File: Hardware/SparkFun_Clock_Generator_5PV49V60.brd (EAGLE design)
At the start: 27.9 x 25.4 mm, 72 parts, among them U1 IDT_5P49V60_CLOCK_GENERATOR, Y1 16MHz

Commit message: Minor adjustments to schematic
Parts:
- moved U$36 0.25 mm to (24.3, 16.0)
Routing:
- net GND: vias 20 -> 21
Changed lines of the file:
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@@
 <drawing>
 <settings>
-<setting alwaysvectorfont="yes"/>
+<setting alwaysvectorfont="no"/>
 <setting verticaltext="up"/>
 </settings>
-<grid distance="0.05" unitdist="inch" unit="inch" style="lines" multiple="1" display="yes" altdistance="0.001" altunitdist="inch" altunit="inch"/>
+<grid distance="0.01" unitdist="inch" unit="inch" style="lines" multiple="1" display="yes" altdistance="0.001" altunitdist="inch" altunit="inch"/>
 <layers>
 <layer number="1" name="Top" color="4" fill="1" visible="yes" active="yes"/>
@@
 <layer number="37" name="tTest" color="7" fill="1" visible="no" active="yes"/>
 <layer number="38" name="bTest" color="7" fill="1" visible="no" active="yes"/>
-<layer number="39" name="tKeepout" color="4" fill="11" visible="yes" active="yes"/>
+<layer number="39" name="tKeepout" color="4" fill="11" visible="no" active="yes"/>
 <layer number="40" name="bKeepout" color="1" fill="11" visible="no" active="yes"/>
 <layer number="41" name="tRestrict" color="4" fill="10" visible="no" active="yes"/>
@@
 <layer number="45" name="Holes" color="7" fill="1" visible="yes" active="yes"/>
 <layer number="46" name="Milling" color="3" fill="1" visible="no" active="yes"/>
-<layer number="47" name="Measures" color="7" fill="1" visible="yes" active="yes"/>
+<layer number="47" name="Measures" color="7" fill="1" visible="no" active="yes"/>
 <layer number="48" name="Document" color="7" fill="1" visible="no" active="yes"/>
 <layer number="49" name="Reference" color="13" fill="1" visible="yes" active="yes"/>
@@
 <element name="U$34" library="Even more labels" package="CLKB13" value="" x="19.939" y="18.3642" smashed="yes" rot="R90"/>
 <element name="U$35" library="Labels" package="I_SUPER2_C-()-03" value="" x="5.7658" y="16.002" smashed="yes" rot="MR0"/>
-<element name="U$36" library="led" package="LED0" value="" x="24.5618" y="16.002" smashed="yes" rot="MR0"/>
+<element name="U$36" library="led" package="LED0" value="" x="24.3078" y="16.002" smashed="yes" rot="MR0"/>
 <element name="J7" library="SparkFun-Connectors" package="1X01_SMALL" value="" x="19.0246" y="20.2184" smashed="yes"/>
 <element name="J8" library="SparkFun-Connectors" package="1X01_SMALL" value="" x="19.05" y="17.78" smashed="yes"/>
@@
 <via x="19.1262" y="18.7452" extent="1-16" drill="0.381"/>
 <via x="16.51" y="20.2946" extent="1-16" drill="0.381"/>
+<via x="16.6116" y="6.4516" extent="1-16" drill="0.381"/>
 </signal>
 <signal name="3.3V">
@@
 <wire x1="15.7988" y1="13.5382" x2="16.7386" y2="12.5984" width="0.2032" layer="16"/>
 <contactref element="J3" pad="8"/>
-<wire x1="24.3332" y1="3.6068" x2="25.008" y2="3.6068" width="0.2032" layer="16"/>
-<wire x1="16.7386" y1="12.5984" x2="16.7386" y2="11.2014" width="0.2032" layer="16"/>
-<wire x1="16.7386" y1="11.2014" x2="24.3332" y2="3.6068" width="0.2032" layer="16"/>
+<wire x1="24.8412" y1="3.6068" x2="25.008" y2="3.6068" width="0.2032" layer="16"/>
+<wire x1="16.7386" y1="12.5984" x2="16.7386" y2="11.7094" width="0.2032" layer="16"/>
+<wire x1="16.7386" y1="11.7094" x2="24.8412" y2="3.6068" width="0.2032" layer="16"/>
 </signal>
 <signal name="OUT1B">

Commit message: Removes pulling SEL_I2CB line from ground, and instead leaves it floating
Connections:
- new net SEL_I2CB: U1.P24
- net GND: no longer U1.P24
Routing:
- net GND: track 13.2 -> 8.49 mm, vias 21 -> 20
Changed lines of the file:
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@@
 <vertex x="-1.27" y="0"/>
 </polygon>
-<contactref element="U1" pad="P24"/>
 <contactref element="J4" pad="1"/>
 <contactref element="J1" pad="1"/>
@@
 <contactref element="C7" pad="2"/>
 <via x="10.3378" y="16.8402" extent="1-16" drill="0.381"/>
-<wire x1="14.6" y1="15.728" x2="14.62" y2="15.748" width="0.254" layer="1"/>
-<wire x1="14.62" y1="15.748" x2="15.5194" y2="15.748" width="0.254" layer="1"/>
-<wire x1="15.5194" y1="15.748" x2="16.129" y2="16.3576" width="0.254" layer="1"/>
 <via x="19.7358" y="12.9794" extent="1-16" drill="0.381"/>
 <via x="23.0632" y="11.2014" extent="1-16" drill="0.381"/>
-<via x="18.2372" y="16.7894" extent="1-16" drill="0.381"/>
 <via x="11.5316" y="21.3106" extent="1-16" drill="0.381"/>
 <via x="6.1214" y="14.9098" extent="1-16" drill="0.381"/>
 <via x="6.0706" y="16.383" extent="1-16" drill="0.381"/>
 <via x="6.3754" y="19.7358" extent="1-16" drill="0.381"/>
-<wire x1="17.8054" y1="16.3576" x2="18.2372" y2="16.7894" width="0.254" layer="1"/>
-<wire x1="16.129" y1="16.3576" x2="17.8054" y2="16.3576" width="0.254" layer="1"/>
 <wire x1="12.7" y1="14.478" x2="11.45" y2="15.728" width="0.254" layer="1"/>
 <wire x1="11.45" y1="15.728" x2="11.45" y2="16.378" width="0.254" layer="1"/>
 <wire x1="12.7" y1="14.478" x2="13.95" y2="15.728" width="0.254" layer="1"/>
-<wire x1="13.95" y1="15.728" x2="14.6" y2="15.728" width="0.254" layer="1"/>
 <via x="19.3802" y="14.1986" extent="1-16" drill="0.381"/>
 <wire x1="11.45" y1="16.378" x2="11.45" y2="16.998" width="0.254" layer="1"/>
@@
 <wire x1="25.4896" y1="18.2372" x2="25.4896" y2="17.3404" width="0.2032" layer="1"/>
 </signal>
+<signal name="SEL_I2CB">
+<contactref element="U1" pad="P24"/>
+</signal>
 </signals>

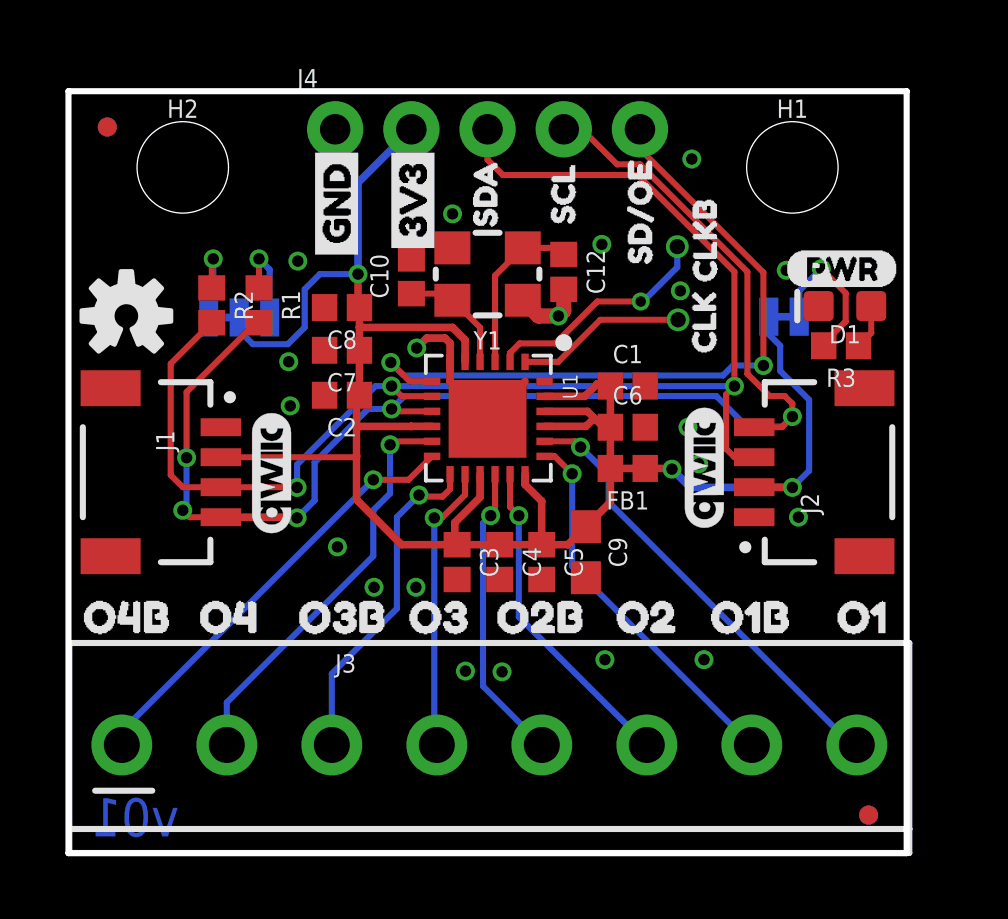
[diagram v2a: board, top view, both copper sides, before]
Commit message: Removes screw terminals in place of PTH header (with additional ground through holes)
* Adds better silk that...just makes more sense
* Adds ground vias to ground pad under IC
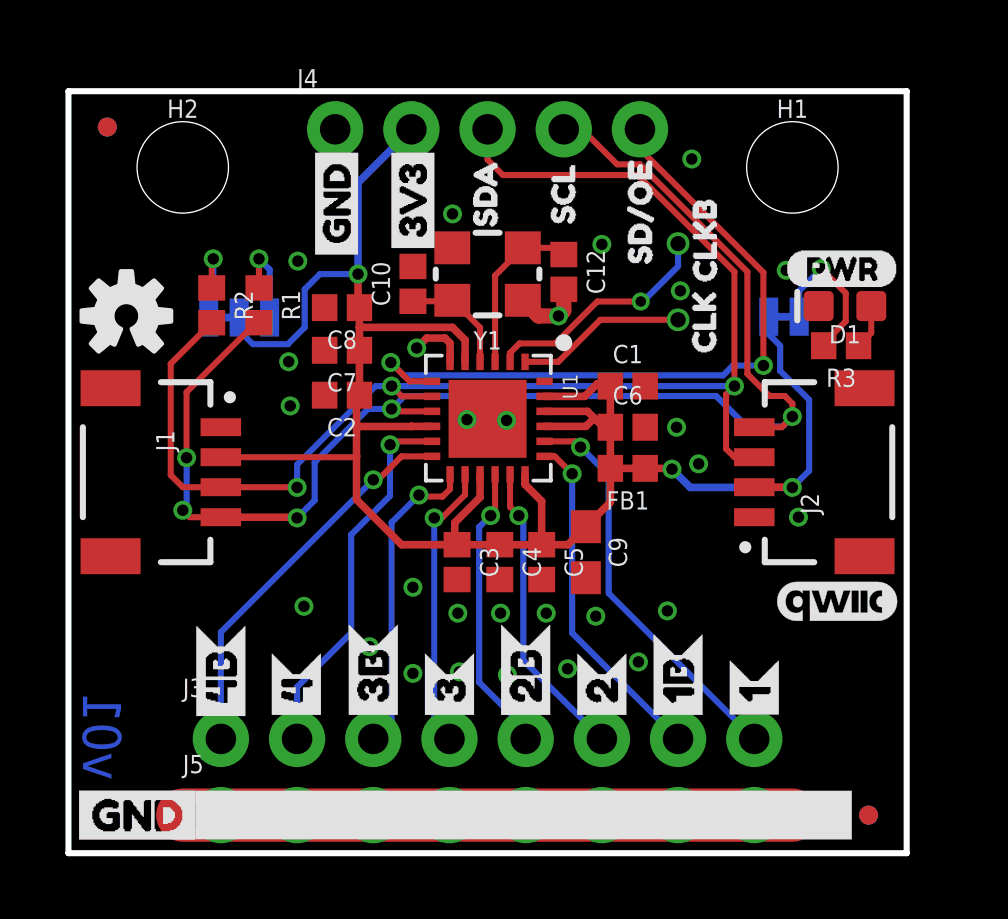
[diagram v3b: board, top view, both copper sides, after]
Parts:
- removed U$1: (no value), SparkFun-Aesthetics:QWIIC_4MM
- added J5: (no value), SparkFun-Connectors:1X08_NO_SILK
- added U$37: (no value), Top clock labels:34
- added U$38: (no value), Top clock labels:46
- J3: device SparkFun-Connectors:SCREWTERMINAL-3.5MM-8 -> SparkFun-Connectors:1X08_NO_SILK
- U$10: device Every Label:O29 -> Bottom Clock Labels:CLK3B5
- U$11: device Every Label:O2B10 -> Bottom Clock Labels:CLK4B7
- U$12: device Every Label:O37 -> Bottom Clock Labels:CLK10
- U$13: device Every Label:O3B8 -> Bottom Clock Labels:CLK22
- U$14: device Every Label:O4B6 -> Bottom Clock Labels:CLK34
- U$15: device Every Label:O45 -> Bottom Clock Labels:CLK46
- U$20: device Even more labels:OUT1B4 -> Labels:GND-04
- U$21: device Even more labels:OUT2B6 -> Labels:GND-04
- U$22: device Even more labels:OUT3B8 -> Top clock labels:1B1
- U$23: device Even more labels:OUT4B10 -> Top clock labels:2B3
- U$24: device Even more labels:OUT13 -> Top clock labels:3B5
- U$25: device Even more labels:OUT25 -> Top clock labels:4B7
- U$26: device Even more labels:OUT37 -> Top clock labels:10
- U$27: device Even more labels:OUT49 -> Top clock labels:22
- U$8: device Every Label:O1B12 -> Bottom Clock Labels:CLK1B1
- U$9: device Every Label:O111 -> Bottom Clock Labels:CLK2B3
- moved U$20 19.7 mm to (3.45, 1.27), turned to 0 degrees
- moved U$21 17.8 mm to (-1.40, 1.27), flipped to the top, turned to 0 degrees
- moved U$24 16.6 mm to (8.89, 4.09), flipped to the top, turned to 90 degrees
- moved U$25 14.8 mm to (3.81, 4.09), flipped to the top, turned to 90 degrees
- moved U$23 14.4 mm to (14.0, 4.09), flipped to the top, turned to 90 degrees
- moved U$27 13.3 mm to (16.5, 4.09), flipped to the top, turned to 90 degrees
- moved U$14 13.1 mm to (11.4, 8.31), flipped to the bottom, turned to 270 degrees
- moved U$22 12.6 mm to (19.1, 4.09), flipped to the top, turned to 90 degrees
- moved U$12 12.4 mm to (21.6, 8.10), flipped to the bottom, turned to 270 degrees
- moved U$26 11.5 mm to (21.6, 4.14), flipped to the top, turned to 90 degrees
- moved U$13 11.1 mm to (16.5, 8.31), flipped to the bottom, turned to 270 degrees
- moved U$9 9.54 mm to (14.0, 8.99), flipped to the bottom, turned to 270 degrees
- moved U$11 8.33 mm to (3.81, 8.97), flipped to the bottom, turned to 270 degrees
- moved U$10 7.27 mm to (8.89, 8.99), flipped to the bottom, turned to 270 degrees
- moved LOGO3 6.29 mm to (24.4, 8.38), turned to 0 degrees
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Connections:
- net GND: now also J5.1, J5.2, J5.3, J5.4, J5.5, J5.6, J5.7, J5.8
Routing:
- net GND: track 8.49 -> 24.6 mm, vias 20 -> 28
- net OUT1: track 15.1 -> 13.4 mm
- net OUT4B: track 14.6 -> 13.0 mm
- net OUT1B: track 12.7 -> 11.5 mm
- net OUT4: track 13.7 -> 12.5 mm
- net OUT2: track 10.9 -> 10.1 mm
- net OUT3B: track 11.2 -> 10.4 mm

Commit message: Moves I2C header to align with bottom header
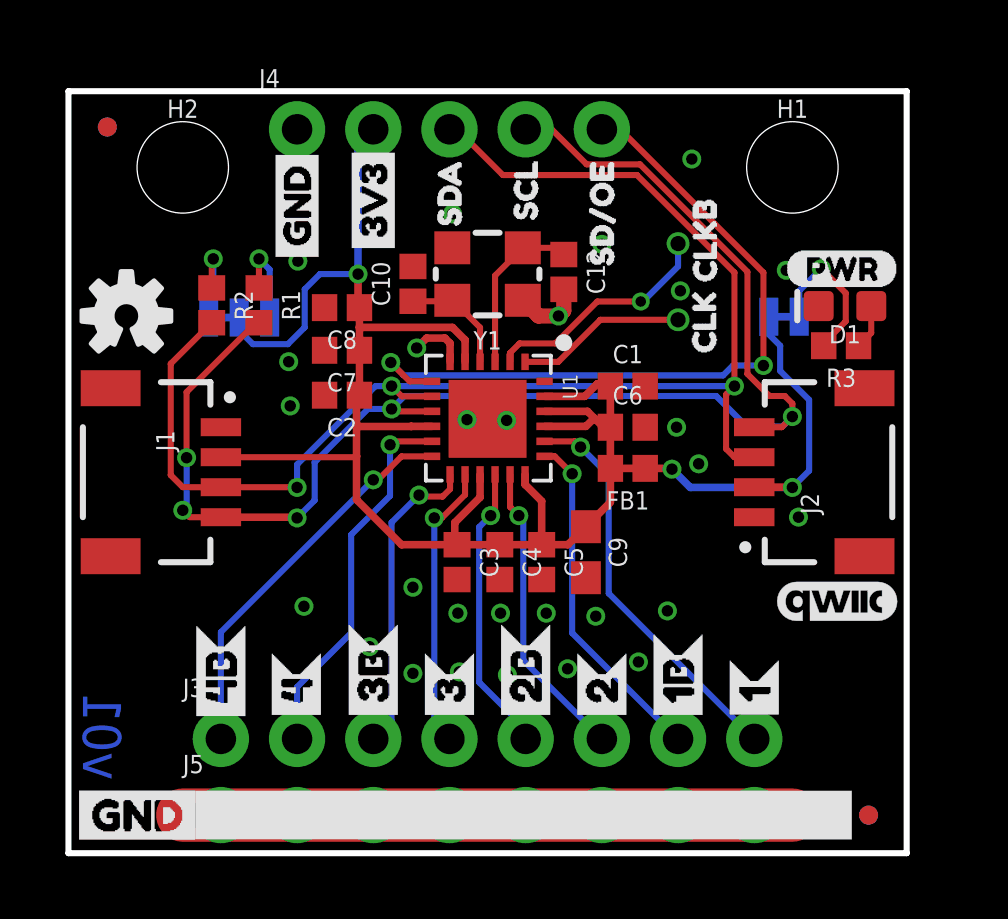
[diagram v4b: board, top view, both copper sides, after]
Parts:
- moved U$18 1.35 mm to (8.89, 23.8)
- moved U$19 1.32 mm to (6.35, 23.7)
- moved U$3 1.32 mm to (6.35, 19.5)
- moved U$2 1.32 mm to (8.89, 19.7)
- moved U$29 1.27 mm to (16.5, 23.7)
- moved U$7 1.27 mm to (16.5, 18.9)
- moved J4 1.27 mm to (6.35, 24.1)
- moved U$6 1.25 mm to (14.0, 20.4)
- moved U$28 1.24 mm to (14.0, 23.6)
- moved U$30 1.22 mm to (11.4, 23.6)
- moved U$5 1.19 mm to (11.4, 20.2)
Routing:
- net SEL0/SCL: track 47.4 -> 48.7 mm
- net SD/OE: track 24.0 -> 24.8 mm
- net SEL1/SDA: track 45.8 -> 46.5 mm
- net 3.3V: track 70.7 -> 70.1 mm
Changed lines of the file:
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@@
 <attribute name="VALUE" x="9.7" y="15.978" size="0.5" layer="27" rot="R270"/>
 </element>
-<element name="J4" library="SparkFun-Connectors" package="1X05_NO_SILK" value="" x="7.62" y="24.13" smashed="yes">
-<attribute name="NAME" x="6.35" y="25.527" size="0.6096" layer="25" font="vector" ratio="20"/>
-<attribute name="VALUE" x="6.35" y="22.098" size="0.6096" layer="27" font="vector" ratio="20"/>
+<element name="J4" library="SparkFun-Connectors" package="1X05_NO_SILK" value="" x="6.35" y="24.13" smashed="yes">
+<attribute name="NAME" x="5.08" y="25.527" size="0.6096" layer="25" font="vector" ratio="20"/>
+<attribute name="VALUE" x="5.08" y="22.098" size="0.6096" layer="27" font="vector" ratio="20"/>
 </element>
 <element name="H1" library="SparkFun-Hardware" package="STAND-OFF-TIGHT" value="STAND-OFFTIGHT" x="22.86" y="22.86" smashed="yes">
@@
 <element name="LOGO2" library="SparkFun-Aesthetics" package="OSHW-LOGO-S" value="OSHW-LOGOS" x="0.6604" y="17.907" smashed="yes"/>
 <element name="LOGO3" library="SparkFun-Aesthetics" package="QWIIC_4MM" value="QWIIC_LOGO_4MM" x="24.3586" y="8.382" smashed="yes"/>
-<element name="U$2" library="Labels" package="3V3-03" value="" x="10.2108" y="19.7104" smashed="yes" rot="R90"/>
-<element name="U$3" library="Labels" package="GND-03" value="" x="7.6708" y="19.5326" smashed="yes" rot="R90"/>
+<element name="U$2" library="Labels" package="3V3-03" value="" x="8.89" y="19.7104" smashed="yes" rot="R90"/>
+<element name="U$3" library="Labels" package="GND-03" value="" x="6.35" y="19.4564" smashed="yes" rot="R90"/>
 <element name="U$4" library="Labels" package="PWR-()-03" value="" x="22.6314" y="19.4818" smashed="yes"/>
-<element name="U$5" library="Every Label" package="SDA11" value="" x="12.6238" y="20.193" smashed="yes" rot="R90"/>
-<element name="U$6" library="Every Label" package="SCL10" value="" x="15.2146" y="20.2946" smashed="yes" rot="R90"/>
-<element name="U$7" library="Every Label" package="SD#OE12" value="" x="17.78" y="18.9484" smashed="yes" rot="R90"/>
+<element name="U$5" library="Every Label" package="SDA11" value="" x="11.43" y="20.2184" smashed="yes" rot="R90"/>
+<element name="U$6" library="Every Label" package="SCL10" value="" x="13.97" y="20.4216" smashed="yes" rot="R90"/>
+<element name="U$7" library="Every Label" package="SD#OE12" value="" x="16.51" y="18.8976" smashed="yes" rot="R90"/>
 <element name="U$16" library="Every Label" package="CLOCK_GENERATOR0" value="" x="19.177" y="13.2842" smashed="yes" rot="MR0"/>
 <element name="U$17" library="Every Label" package="5PV49V601" value="" x="17.4752" y="11.5316" smashed="yes" rot="MR0"/>
-<element name="U$18" library="Labels" package="3V3-03" value="" x="10.2362" y="23.8252" smashed="yes" rot="MR270"/>
-<element name="U$19" library="Labels" package="GND-03" value="" x="7.6708" y="23.7744" smashed="yes" rot="MR270"/>
-<element name="U$28" library="Even more labels" package="SCL1" value="" x="15.2146" y="23.6474" smashed="yes" rot="MR270"/>
-<element name="U$29" library="Even more labels" package="SD#OE2" value="" x="17.78" y="23.622" smashed="yes" rot="MR270"/>
-<element name="U$30" library="Even more labels" package="SDA0" value="" x="12.6492" y="23.622" smashed="yes" rot="MR270"/>
+<element name="U$18" library="Labels" package="3V3-03" value="" x="8.89" y="23.7998" smashed="yes" rot="MR270"/>
+<element name="U$19" library="Labels" package="GND-03" value="" x="6.35" y="23.6982" smashed="yes" rot="MR270"/>
+<element name="U$28" library="Even more labels" package="SCL1" value="" x="13.97" y="23.6474" smashed="yes" rot="MR270"/>
+<element name="U$29" library="Even more labels" package="SD#OE2" value="" x="16.51" y="23.6728" smashed="yes" rot="MR270"/>
+<element name="U$30" library="Even more labels" package="SDA0" value="" x="11.43" y="23.6474" smashed="yes" rot="MR270"/>
 <element name="U$32" library="Even more labels" package="CLK11" value="" x="19.9644" y="19.5072" smashed="yes" rot="MR270"/>
 <element name="U$31" library="Even more labels" package="CLKB13" value="" x="19.9898" y="22.3774" smashed="yes" rot="MR270"/>
@@
 <wire x1="8.382" y1="18.233" x2="8.382" y2="19.304" width="0.254" layer="1"/>
 <via x="8.382" y="19.304" extent="1-16" drill="0.381"/>
-<wire x1="8.382" y1="19.304" x2="8.382" y2="22.352" width="0.254" layer="16"/>
-<wire x1="8.382" y1="22.352" x2="10.16" y2="24.13" width="0.254" layer="16"/>
+<wire x1="8.382" y1="19.304" x2="8.382" y2="23.622" width="0.254" layer="16"/>
+<wire x1="8.382" y1="23.622" x2="8.89" y2="24.13" width="0.254" layer="16"/>
 <wire x1="4.4196" y1="17.8562" x2="4.4196" y2="17.4244" width="0.2032" layer="16"/>
 <wire x1="4.4196" y1="17.4244" x2="4.8768" y2="16.9672" width="0.2032" layer="16"/>
@@
 <wire x1="20.9296" y1="13.2" x2="21.59" y2="13.2" width="0.2032" layer="1"/>
 <wire x1="9.4996" y1="15.5702" x2="20.9296" y2="15.5702" width="0.2032" layer="16"/>
-<wire x1="13.208" y1="22.606" x2="12.7" y2="23.114" width="0.2032" layer="1"/>
-<wire x1="12.7" y1="23.114" x2="12.7" y2="24.13" width="0.2032" layer="1"/>
+<wire x1="13.208" y1="22.606" x2="11.684" y2="24.13" width="0.2032" layer="1"/>
+<wire x1="11.684" y1="24.13" x2="11.43" y2="24.13" width="0.2032" layer="1"/>
 <wire x1="20.9296" y1="15.5702" x2="20.6502" y2="15.2908" width="0.2032" layer="1"/>
 <wire x1="20.6502" y1="13.4794" x2="20.9296" y2="13.2" width="0.2032" layer="1"/>
@@
 <wire x1="2.1376" y1="12.6024" x2="2.1376" y2="16.315" width="0.2032" layer="1"/>
 <wire x1="2.1376" y1="16.315" x2="3.5052" y2="17.6826" width="0.2032" layer="1"/>
-<wire x1="20.9296" y1="15.5702" x2="20.9296" y2="19.3802" width="0.2032" layer="1"/>
-<wire x1="20.9296" y1="19.3802" x2="17.7038" y2="22.606" width="0.2032" layer="1"/>
-<wire x1="17.7038" y1="22.606" x2="13.208" y2="22.606" width="0.2032" layer="1"/>
+<wire x1="20.9296" y1="15.5702" x2="20.9296" y2="19.3548" width="0.2032" layer="1"/>
+<wire x1="20.9296" y1="19.3548" x2="17.6784" y2="22.606" width="0.2032" layer="1"/>
+<wire x1="17.6784" y1="22.606" x2="13.208" y2="22.606" width="0.2032" layer="1"/>
 </signal>
 <signal name="SEL0/SCL">
@@
 <wire x1="6.9342" y1="11.7602" x2="6.35" y2="11.176" width="0.2032" layer="16"/>
 <via x="22.86" y="14.5542" extent="1-16" drill="0.381"/>
-<wire x1="15.8496" y1="24.13" x2="15.24" y2="24.13" width="0.2032" layer="1"/>
+<wire x1="14.8336" y1="24.13" x2="13.97" y2="24.13" width="0.2032" layer="1"/>
 <wire x1="9.4996" y1="14.8082" x2="9.9314" y2="15.24" width="0.2032" layer="16"/>
 <wire x1="9.9314" y1="15.24" x2="20.32" y2="15.24" width="0.2032" layer="16"/>
@@
 <wire x1="22.86" y1="14.986" x2="22.86" y2="14.5542" width="0.2032" layer="1"/>
 <wire x1="21.3614" y1="15.9766" x2="22.098" y2="15.24" width="0.2032" layer="1"/>
-<wire x1="15.8496" y1="24.13" x2="17.018" y2="22.9616" width="0.2032" layer="1"/>
-<wire x1="17.018" y1="22.9616" x2="17.78" y2="22.9616" width="0.2032" layer="1"/>
+<wire x1="14.8336" y1="24.13" x2="16.002" y2="22.9616" width="0.2032" layer="1"/>
+<wire x1="16.002" y1="22.9616" x2="17.78" y2="22.9616" width="0.2032" layer="1"/>
 <wire x1="17.78" y1="22.9616" x2="21.3614" y2="19.3802" width="0.2032" layer="1"/>
 <wire x1="21.3614" y1="19.3802" x2="21.3614" y2="15.9766" width="0.2032" layer="1"/>
@@
 <wire x1="20.8788" y1="16.256" x2="21.8948" y2="16.256" width="0.2032" layer="16"/>
 <wire x1="21.8948" y1="16.256" x2="21.8948" y2="19.3548" width="0.2032" layer="1"/>
-<wire x1="17.78" y1="23.4696" x2="17.78" y2="24.13" width="0.2032" layer="1"/>
-<wire x1="21.8948" y1="19.3548" x2="17.78" y2="23.4696" width="0.2032" layer="1"/>
+<wire x1="17.1196" y1="24.13" x2="16.51" y2="24.13" width="0.2032" layer="1"/>
+<wire x1="21.8948" y1="19.3548" x2="17.1196" y2="24.13" width="0.2032" layer="1"/>
 </signal>
 <signal name="CLKIN">
